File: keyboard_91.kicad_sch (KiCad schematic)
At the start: 43 parts, among them J1 SW_Cherry_MX_1.00u_Plate, K1 SW_Cherry_MX_1.00u_Plate, M1 SW_Cherry_MX_1.00u_Plate, P1 SW_Cherry_MX_1.00u_Plate, Q1 SW_Cherry_MX_1.00u_Plate, T1 SW_Cherry_MX_1.00u_Plate, U1 SW_Cherry_MX_1.00u_Plate, X1 SW_Cherry_MX_1.00u_Plate, Y1 SW_Cherry_MX_1.00u_Plate

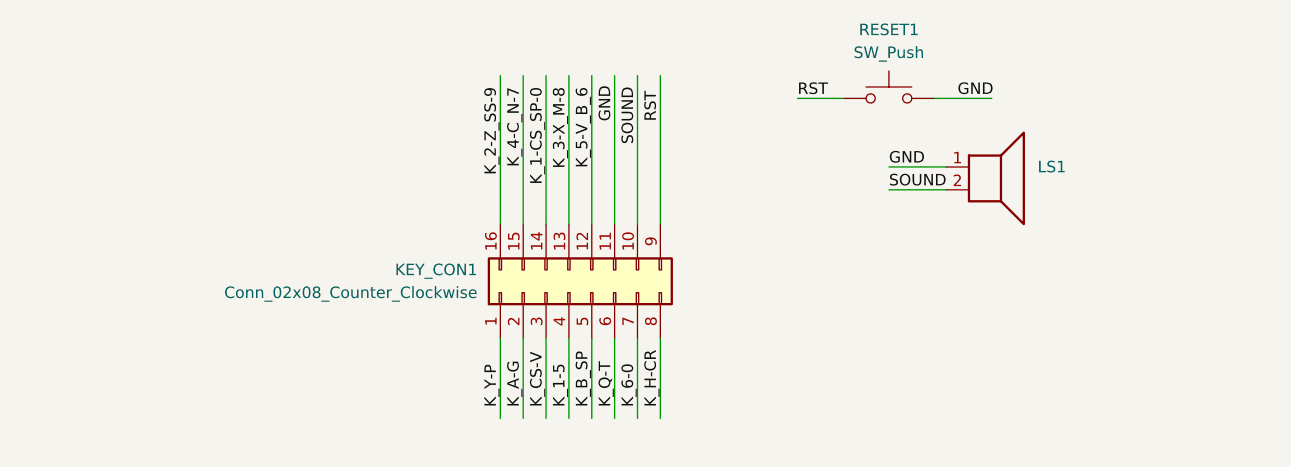
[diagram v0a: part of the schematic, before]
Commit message: Moure touches
- hide useless stuff
- add reset buttons SIP
- add speaker SIP
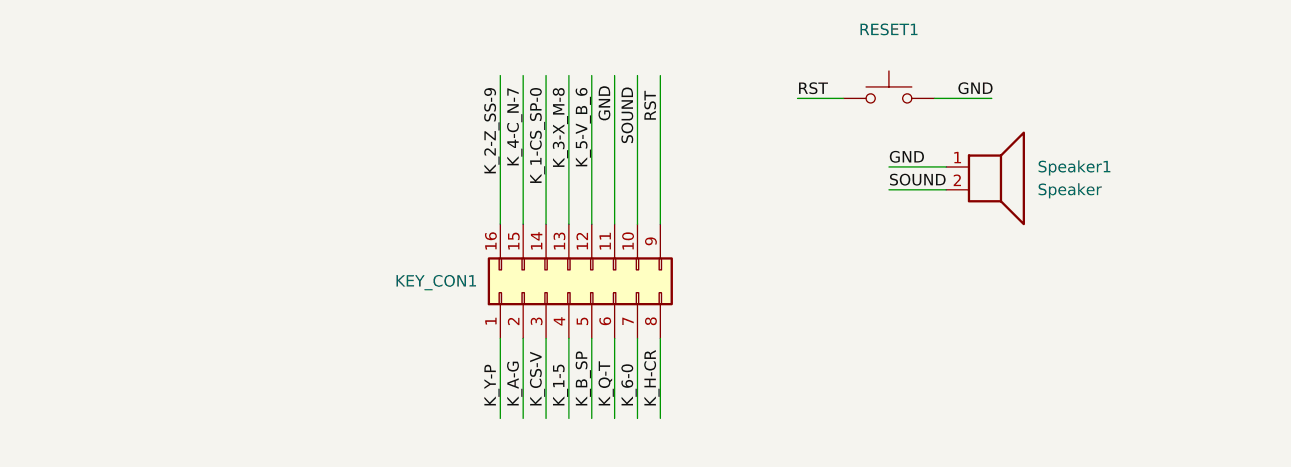
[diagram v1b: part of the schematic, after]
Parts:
- KEY_CON1: value Conn_02x08_Counter_Clockwise -> (none)
- RESET1: value SW_Push -> (none)
- Speaker1: renamed from LS1; value (none) -> Speaker; footprint (none) -> Library:SIP-2
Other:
- title: HC91 Keyboard -> HC 85,90,91 Cherry MX PCB
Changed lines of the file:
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@@
   (paper "A4")
   (title_block
-    (title "HC91 Keyboard")
-    (rev "v1")
+    (title "HC 85,90,91 Cherry MX PCB")
+    (date "2022-04-19")
+    (rev "1")
     (company "https://zx.licentia.eu")
-    (comment 1 "HC 91, 40 keys keyboard")
+    (comment 1 "40 Keys Cherry MX PCB")
   )
   (junction (at 76.2 95.25) (diameter 0) (color 0 0 0 0)
@@
   (symbol (lib_id "Connector_Generic:Conn_02x08_Counter_Clockwise") (at 110.49 43.18 90) (unit 1)
     (in_bom yes) (on_board yes) (fields_autoplaced)
-    (property "Reference" "KEY_CON1" (id 0) (at 100.33 40.6399 90)
+    (property "Reference" "KEY_CON1" (id 0) (at 100.33 41.9099 90)
       (effects (font (size 1.27 1.27)) (justify left))
     )
-    (property "Value" "Conn_02x08_Counter_Clockwise" (id 1) (at 100.33 43.1799 90)
-      (effects (font (size 1.27 1.27)) (justify left))
+    (property "Value" "" (id 1) (at 100.33 43.1799 90)
+      (effects (font (size 1.27 1.27)) (justify left) hide)
     )
     (property "Footprint" "Library:DIP-16_276" (id 2) (at 110.49 43.18 0)
@@
   (symbol (lib_id "Device:Speaker") (at 157.48 29.21 0) (unit 1)
     (in_bom yes) (on_board yes) (fields_autoplaced)
-    (property "Reference" "LS1" (id 0) (at 162.56 29.2099 0)
+    (property "Reference" "Speaker1" (id 0) (at 162.56 29.2099 0)
       (effects (font (size 1.27 1.27)) (justify left))
     )
-    (property "Value" "" (id 1) (at 162.56 31.7499 0)
+    (property "Value" "Speaker" (id 1) (at 162.56 31.7499 0)
       (effects (font (size 1.27 1.27)) (justify left))
     )
-    (property "Footprint" "" (id 2) (at 157.48 34.29 0)
+    (property "Footprint" "Library:SIP-2" (id 2) (at 157.48 34.29 0)
       (effects (font (size 1.27 1.27)) hide)
     )
@@
     (in_bom yes) (on_board yes) (fields_autoplaced)
     (property "Reference" "RESET1" (id 0) (at 146.05 13.97 0))
-    (property "Value" "SW_Push" (id 1) (at 146.05 16.51 0))
+    (property "Value" "" (id 1) (at 146.05 16.51 0))
     (property "Footprint" "" (id 2) (at 146.05 16.51 0)
       (effects (font (size 1.27 1.27)) hide)
@@
       (reference "L1") (unit 1) (value "SW_Cherry_MX_1.00u_Plate") (footprint "Button_Switch_Keyboard:SW_Cherry_MX_1.00u_Plate")
     )
-    (path "/916ec44c-162e-4efe-9356-b7f8b461290d"
-      (reference "LS1") (unit 1) (value "Speaker") (footprint "Library:SIP-2")
-    )
     (path "/857d63e5-3418-478e-9b93-b658fd19cf95"
       (reference "M1") (unit 1) (value "SW_Cherry_MX_1.00u_Plate") (footprint "Button_Switch_Keyboard:SW_Cherry_MX_1.00u_Plate")
@@
     )
     (path "/e8fb4f67-b4ca-47ed-95a2-2aefb2346b30"
-      (reference "RESET1") (unit 1) (value "SW_Push") (footprint "")
+      (reference "RESET1") (unit 1) (value "RESET") (footprint "Library:SIP-2")
     )
     (path "/fdc93240-62aa-421a-8034-c3b0a831931d"
@@
       (reference "SS1") (unit 1) (value "SW_Cherry_MX_1.00u_Plate") (footprint "Button_Switch_Keyboard:SW_Cherry_MX_1.00u_Plate")
     )
+    (path "/916ec44c-162e-4efe-9356-b7f8b461290d"
+      (reference "Speaker1") (unit 1) (value "Speaker") (footprint "Library:SIP-2")
+    )
     (path "/c2b57010-d802-4699-ae2a-f7ebf104fef4"

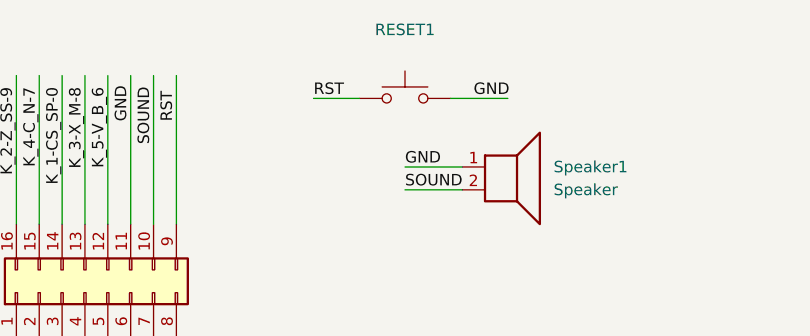
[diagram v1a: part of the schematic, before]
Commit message: Second try
- fixed cherry mx holes (make them 0.8 mm)
- fixed connector holes
- fixed  sound & reset holes
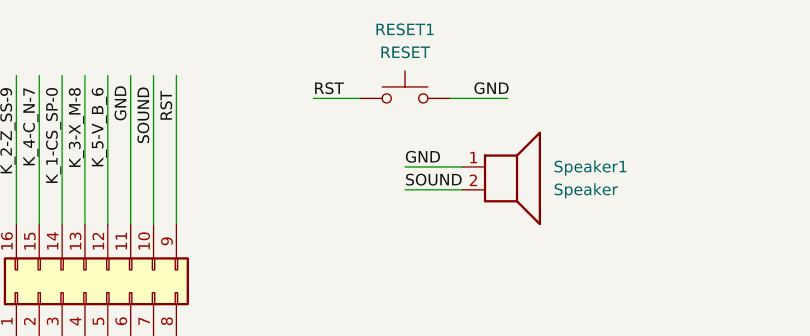
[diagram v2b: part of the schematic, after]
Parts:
- A1, B1, C1, CR1, CS1, D1, E1, F1, G1, H1, I1, J1, K1, L1, M1, N1, O1, P1, Q1, R1, S1, SP1, SS1, T1, U1, V1, W1, X1, Y1, Z1, _0, _1, _2, _3, _4, _5, _6, _7, _8, _9: value SW_Cherry_MX_1.00u_Plate -> SW_Cherry_MX_0.80u_Plate; footprint Button_Switch_Keyboard:SW_Cherry_MX_1.00u_Plate -> Library:SW_Cherry_MX_0.80u_Plate
- KEY_CON1: value (none) -> Conn_02x08_Counter_Clockwise
- RESET1: value (none) -> RESET; footprint (none) -> Library:SIP-2
